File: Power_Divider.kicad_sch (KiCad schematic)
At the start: 31 parts, among them J86 Molex 73251-1153, J93 PIC-S-201F, P602 CONUFL001-SMD-T, P603 CONUFL001-SMD-T, P604 CONUFL001-SMD-T, P609 CONUFL001-SMD-T, U604 RBP-140+, U87 QPL9547

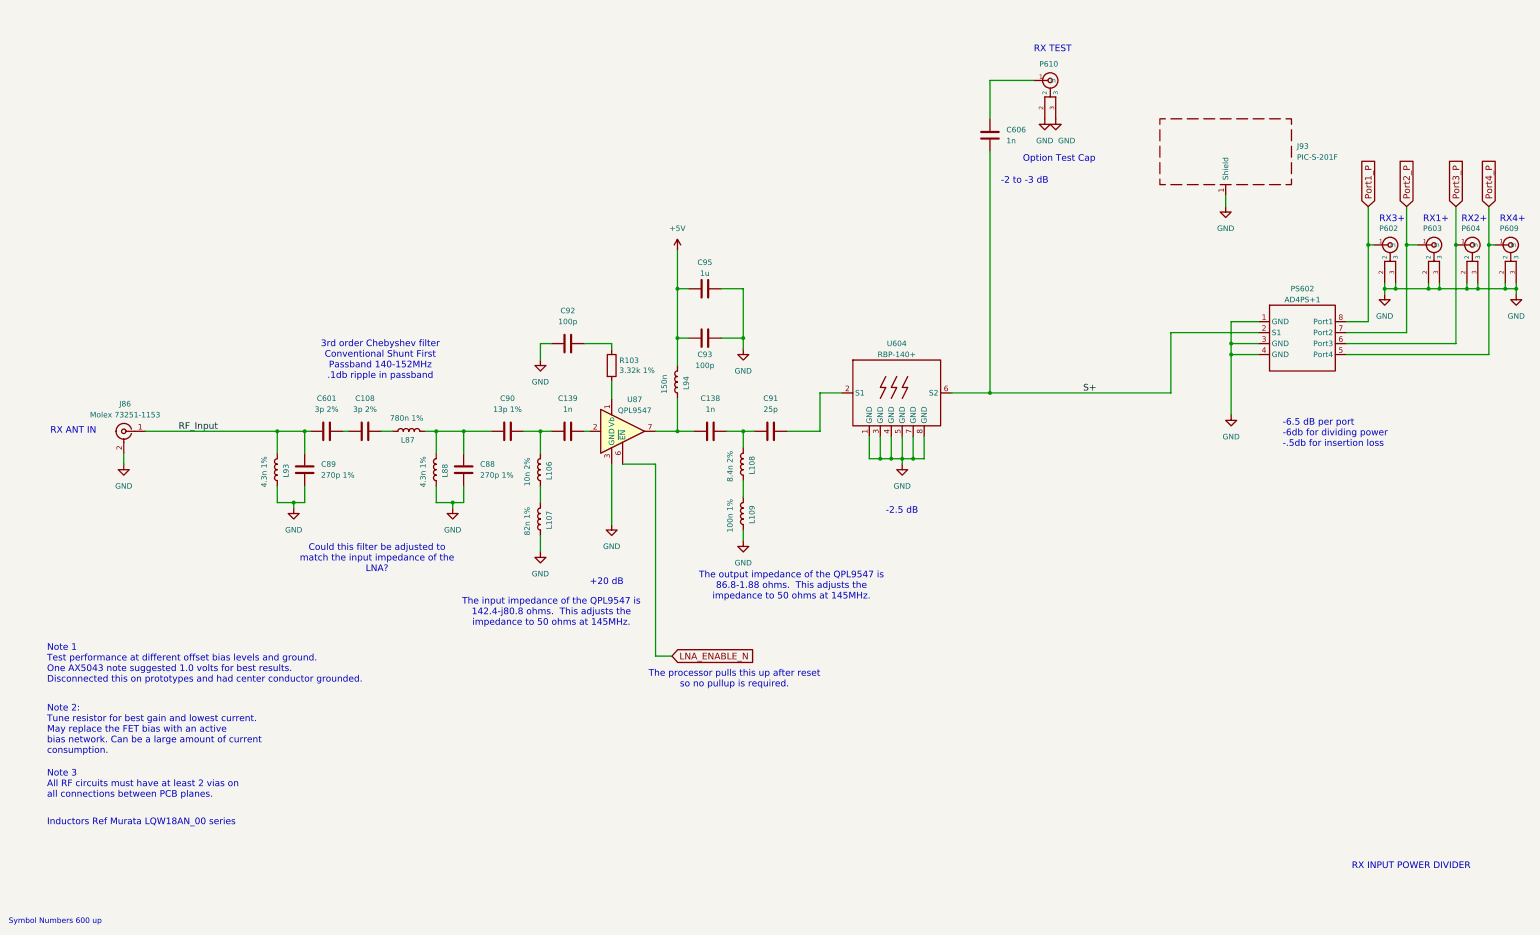
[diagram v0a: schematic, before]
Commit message: Re-annotate all parts
And get rid of the per-sheet annotation remarks.

Signed-off-by: Corey Minyard <corey@minyard.net>
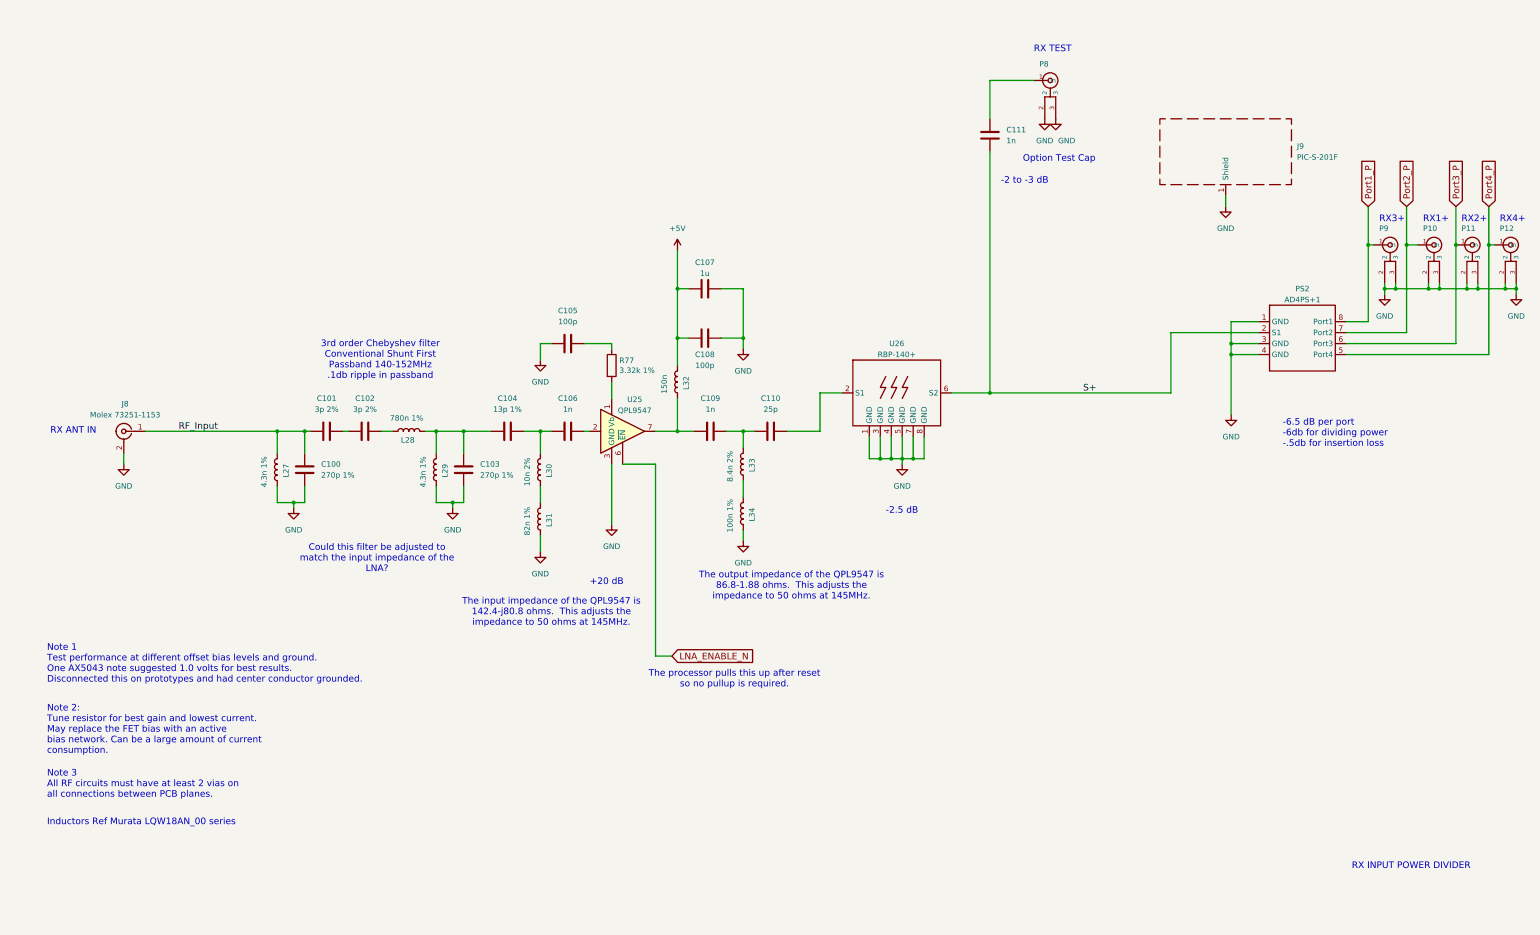
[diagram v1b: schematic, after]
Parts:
- renumbered C89 to C100, C601 to C101, C108 to C102, C88 to C103, C90 to C104, C92 to C105, C139 to C106, C95 to C107, C93 to C108, C138 to C109, C91 to C110, C606 to C111, J86 to J8, J93 to J9, L93 to L27, L87 to L28, L88 to L29, L106 to L30, L107 to L31, L94 to L32, L108 to L33, L109 to L34, P603 to P10, P604 to P11, P609 to P12, P610 to P8, P602 to P9, PS602 to PS2, R103 to R77, U87 to U25, U604 to U26
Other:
- note removed: "Symbol Numbers 600 up"

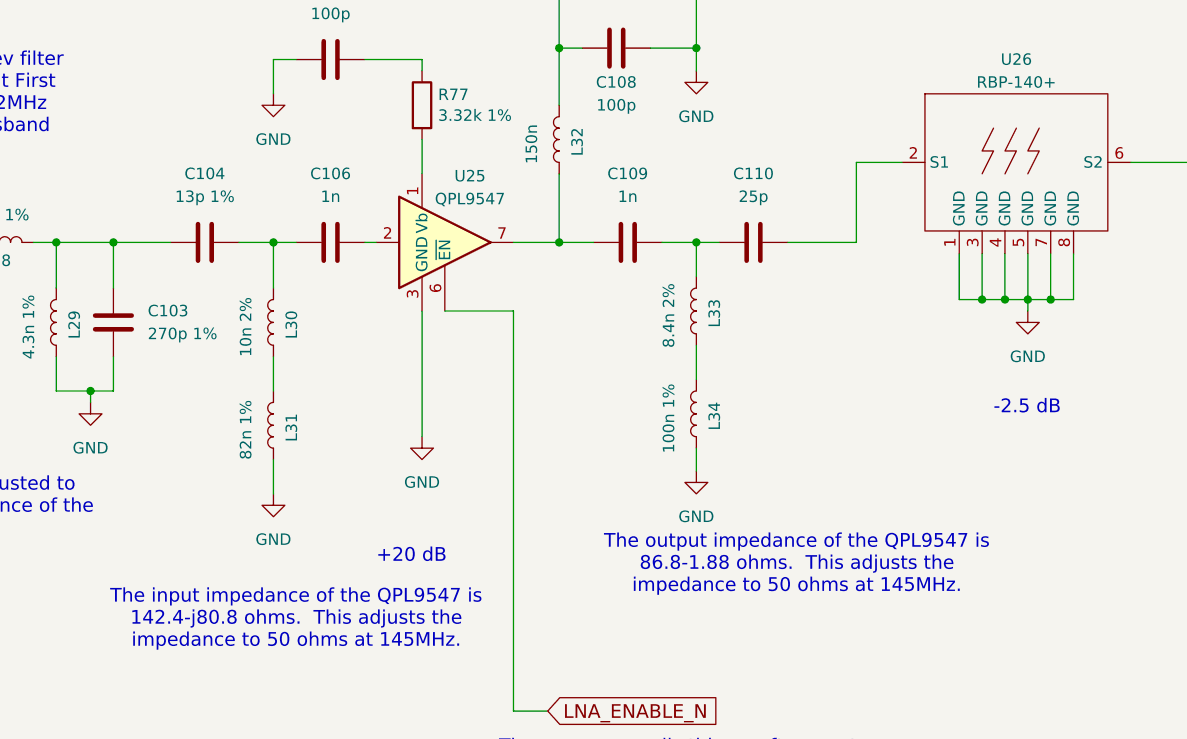
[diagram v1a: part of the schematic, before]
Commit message: Rework the LNA impedance matching
Signed-off-by: Corey Minyard <corey@minyard.net>
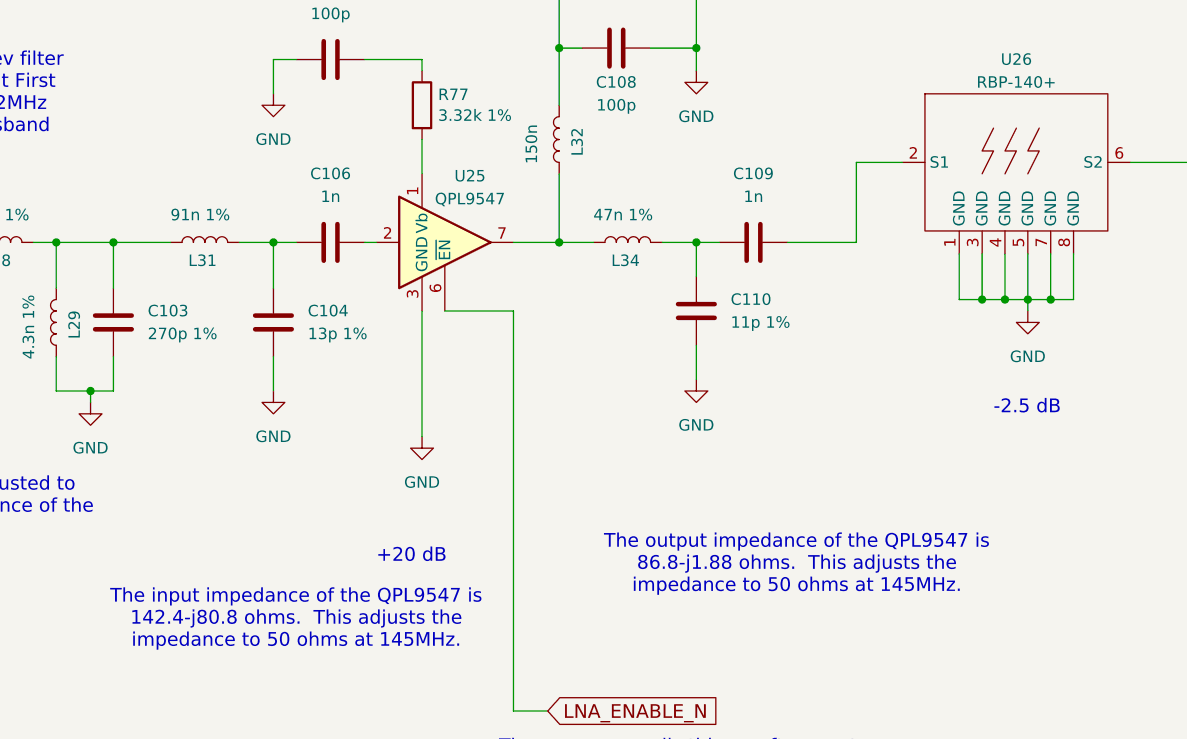
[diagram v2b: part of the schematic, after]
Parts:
- removed L30: 10n 2%, Inductor_SMD:L_0402_1005Metric_Pad0.77x0.64mm_HandSolder, symbol Device:L
- removed L33: 8.4n 2%, Inductor_SMD:L_0402_1005Metric_Pad0.77x0.64mm_HandSolder, symbol Device:L
- C110: value 25p -> 11p 1%
- L31: value 82n 1% -> 91n 1%
- L34: value 100n 1% -> 47n 1%
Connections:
- net GND: now also C104.2, C110.1; no longer L31.2, L34.2
- net at L31.1: now also C104.1, C106.2
- net at L32.2, U25.7: now also L34.2; no longer C109.2
- net at C109.1: now also U26.2 (S1); no longer C110.2
- net at C103.2, L28.1, L29.1: now also L31.2; no longer C104.2
- net at L34.1: now also C109.2, C110.2
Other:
- note added: "The output impedance of the QPL9547 is 86.8-j1.88 ohms. This adjusts the impedance to 50 ohms at 145MHz."
- note removed: "The output impedance of the QPL9547 is 86.8-1.88 ohms. This adjusts the impedance to 50 ohms at 145MHz."
- moved on the sheet: C104, C109, C110, L31, L34

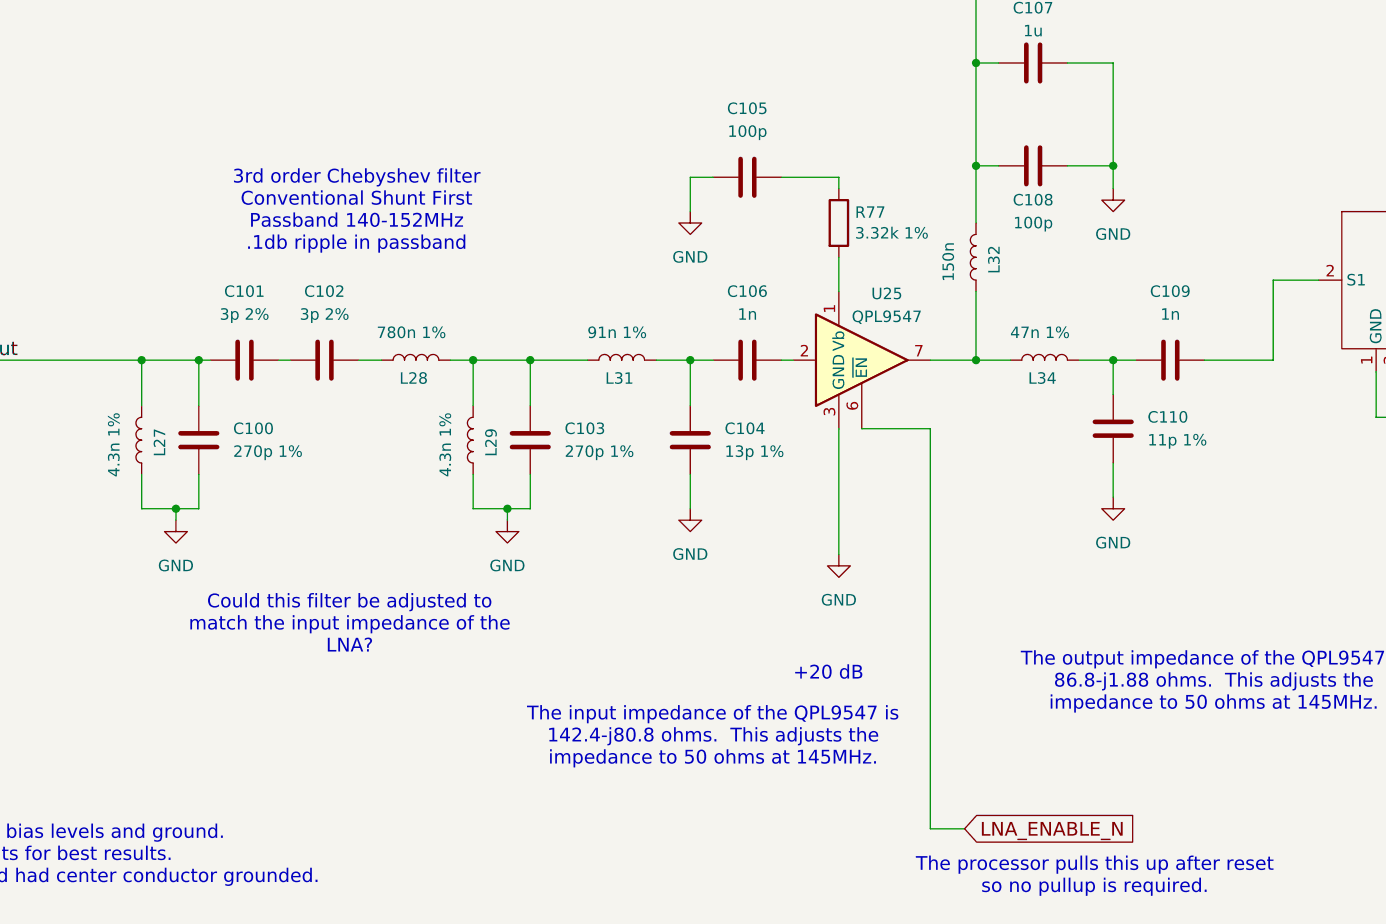
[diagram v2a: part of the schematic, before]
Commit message: More cleanup around the LNA
Had the C/L order on the output impedance match wrong.

Change the double 3pf caps to a 1.5pf, I think a suitable one can be
found.

Signed-off-by: Corey Minyard <corey@minyard.net>
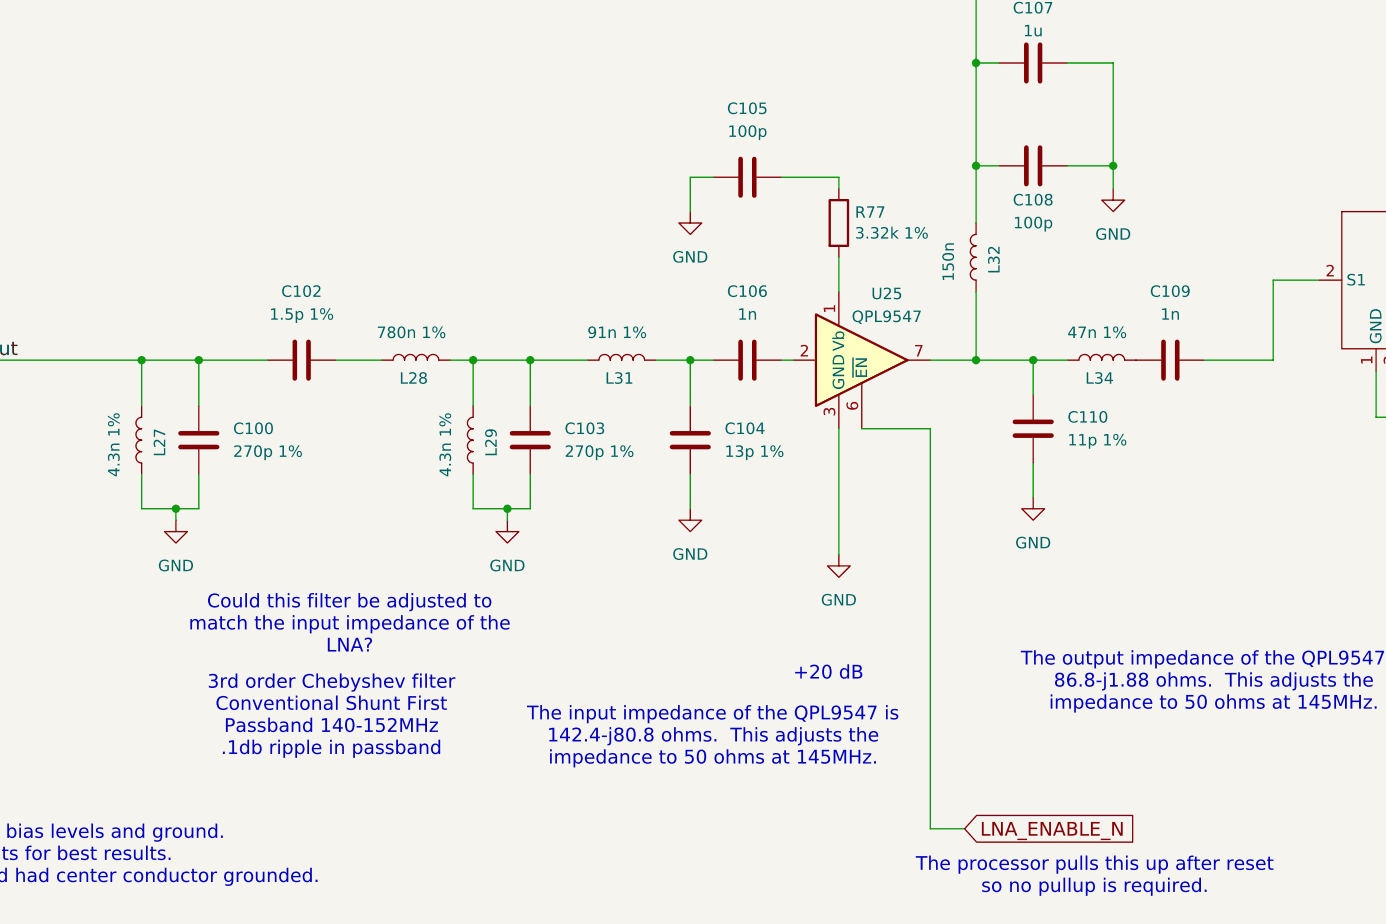
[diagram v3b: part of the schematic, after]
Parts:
- removed C101: 3p 2%, Capacitor_SMD:C_0402_1005Metric_Pad0.74x0.62mm_HandSolder, symbol Device:C
- C102: value 3p 2% -> 1.5p 1%
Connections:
- net RF_Input: now also C102.2
- net at L32.2, L34.2, U25.7: now also C110.2
- net at C109.2, L34.1: no longer C110.2
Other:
- moved on the sheet: C102, C110, L34
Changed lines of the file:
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@@
 	(text "3rd order Chebyshev filter\nConventional Shunt First\nPassband 140-152MHz\n.1db ripple in passband\n"
 		(exclude_from_sim no)
-		(at 105.156 127 0)
+		(at 102.362 183.134 0)
 		(effects
 			(font
@@
 	)
 	(junction
+		(at 87.63 143.51)
+		(diameter 0)
+		(color 0 0 0 0)
+	)
+	(junction
 		(at 302.26 125.73)
 		(diameter 0)
@@
 	)
 	(junction
-		(at 189.23 143.51)
+		(at 180.34 143.51)
 		(diameter 0)
 		(color 0 0 0 0)
@@
 	)
 	(junction
-		(at 87.63 143.51)
-		(diameter 0)
-		(color 0 0 0 0)
-	)
-	(junction
 		(at 246.38 134.62)
 		(diameter 0)
@@
 	(wire
 		(pts
-			(xy 189.23 143.51) (xy 191.77 143.51)
+			(xy 180.34 143.51) (xy 184.15 143.51)
 		)
 		(stroke
@@
 	(wire
 		(pts
-			(xy 189.23 143.51) (xy 189.23 147.32)
+			(xy 180.34 143.51) (xy 180.34 147.32)
 		)
 		(stroke
@@
 	(wire
 		(pts
+			(xy 87.63 143.51) (xy 95.25 143.51)
+		)
+		(stroke
+			(width 0)
+			(type default)
+		)
+	)
+	(wire
+		(pts
 			(xy 328.93 120.65) (xy 342.9 120.65)
 		)
@@
 	(wire
 		(pts
-			(xy 105.41 143.51) (xy 107.95 143.51)
+			(xy 102.87 143.51) (xy 107.95 143.51)
 		)
 		(stroke
@@
 	(wire
 		(pts
-			(xy 189.23 154.94) (xy 189.23 158.75)
+			(xy 180.34 154.94) (xy 180.34 158.75)
 		)
 		(stroke
@@
 	(wire
 		(pts
-			(xy 185.42 143.51) (xy 189.23 143.51)
-		)
-		(stroke
-			(width 0)
-			(type default)
-		)
-	)
-	(wire
-		(pts
 			(xy 142.24 156.21) (xy 142.24 160.02)
 		)
@@
 	(wire
 		(pts
-			(xy 173.99 143.51) (xy 177.8 143.51)
+			(xy 173.99 143.51) (xy 180.34 143.51)
 		)
 		(stroke
@@
 	(wire
 		(pts
-			(xy 87.63 143.51) (xy 88.9 143.51)
-		)
-		(stroke
-			(width 0)
-			(type default)
-		)
-	)
-	(wire
-		(pts
 			(xy 168.91 151.13) (xy 168.91 195.58)
 		)
@@
 	(wire
 		(pts
-			(xy 96.52 143.51) (xy 97.79 143.51)
-		)
-		(stroke
-			(width 0)
-			(type default)
-		)
-	)
-	(wire
-		(pts
 			(xy 223.52 144.78) (xy 223.52 149.86)
 		)
@@
 	(symbol
 		(lib_id "power:GND")
-		(at 189.23 158.75 0)
+		(at 180.34 158.75 0)
 		(unit 1)
 		(exclude_from_sim no)
@@
 		(fields_autoplaced yes)
 		(property "Reference" "#PWR0212"
-			(at 189.23 165.1 0)
+			(at 180.34 165.1 0)
 			(effects
 				(font
@@
 		)
 		(property "Value" "GND"
-			(at 189.23 163.83 0)
+			(at 180.34 163.83 0)
 			(effects
 				(font
@@
 		)
 		(property "Footprint" ""
-			(at 189.23 158.75 0)
+			(at 180.34 158.75 0)
 			(effects
 				(font
@@
 		)
 		(property "Datasheet" ""
-			(at 189.23 158.75 0)
+			(at 180.34 158.75 0)
 			(effects
 				(font
@@
 		)
 		(property "Description" ""
-			(at 189.23 158.75 0)
+			(at 180.34 158.75 0)
 			(effects
 				(font
@@
 	(symbol
 		(lib_id "Device:C")
-		(at 189.23 151.13 180)
+		(at 180.34 151.13 180)
 		(unit 1)
 		(exclude_from_sim no)
@@
 		(fields_autoplaced yes)
 		(property "Reference" "C110"
-			(at 193.04 149.8599 0)
+			(at 184.15 149.8599 0)
 			(effects
 				(font
@@
 		)
 		(property "Value" "11p 1%"
-			(at 193.04 152.3999 0)
+			(at 184.15 152.3999 0)
 			(effects
 				(font
@@
 		)
 		(property "Footprint" "Capacitor_SMD:C_0402_1005Metric_Pad0.74x0.62mm_HandSolder"
-			(at 188.2648 147.32 0)
+			(at 179.3748 147.32 0)
 			(effects
 				(font
@@
 		)
 		(property "Datasheet" "~"
-			(at 189.23 151.13 0)
+			(at 180.34 151.13 0)
 			(effects
 				(font
@@
 		)
 		(property "Description" ""
-			(at 189.23 151.13 0)
+			(at 180.34 151.13 0)
 			(effects
 				(font
@@
 	(symbol
 		(lib_id "Device:L")
-		(at 181.61 143.51 270)
+		(at 187.96 143.51 270)
 		(mirror x)
 		(unit 1)
@@
 		(dnp no)
 		(property "Reference" "L34"
-			(at 181.356 145.542 90)
+			(at 187.706 145.542 90)
 			(effects
 				(font
@@
 		)
 		(property "Value" "47n 1%"
-			(at 181.102 140.462 90)
+			(at 187.452 140.462 90)
 			(effects
 				(font
@@
 		)
 		(property "Footprint" "Inductor_SMD:L_0402_1005Metric_Pad0.77x0.64mm_HandSolder"
-			(at 181.61 143.51 0)
+			(at 187.96 143.51 0)
 			(effects
 				(font
@@
 		)
 		(property "Datasheet" "~"
-			(at 181.61 143.51 0)
+			(at 187.96 143.51 0)
 			(effects
 				(font
@@
 		)
 		(property "Description" ""
-			(at 181.61 143.51 0)
+			(at 187.96 143.51 0)
 			(effects
 				(font
@@
 	(symbol
 		(lib_id "Device:C")
-		(at 101.6 143.51 270)
+		(at 99.06 143.51 270)
 		(unit 1)
 		(exclude_from_sim no)
@@
 		(fields_autoplaced yes)
 		(property "Reference" "C102"
-			(at 101.6 135.89 90)
+			(at 99.06 135.89 90)
 			(effects
 				(font
@@
 			)
 		)
-		(property "Value" "3p 2%"
-			(at 101.6 138.43 90)
+		(property "Value" "1.5p 1%"
+			(at 99.06 138.43 90)
 			(effects
 				(font
@@
 		)
 		(property "Footprint" "Capacitor_SMD:C_0402_1005Metric_Pad0.74x0.62mm_HandSolder"
-			(at 97.79 144.4752 0)
+			(at 95.25 144.4752 0)
 			(effects
 				(font
@@
 		)
 		(property "Datasheet" "~"
-			(at 101.6 143.51 0)
+			(at 99.06 143.51 0)
 			(effects
 				(font
@@
 		)
 		(property "Description" ""
-			(at 101.6 143.51 0)
+			(at 99.06 143.51 0)
 			(effects
 				(font
@@
 					(unit 1)
 				)
-			)
-		)
-	)
-	(symbol
-		(lib_id "Device:C")
-		(at 92.71 143.51 270)
-		(unit 1)
-		(exclude_from_sim no)
-		(in_bom yes)
-		(on_board yes)
-		(dnp no)
-		(fields_autoplaced yes)
-		(property "Reference" "C101"
-			(at 92.71 135.89 90)
-			(effects
-				(font
-					(size 1.27 1.27)
-				)
-			)
-		)
-		(property "Value" "3p 2%"
-			(at 92.71 138.43 90)
-			(effects
-				(font
-					(size 1.27 1.27)
-				)
-			)
-		)
-		(property "Footprint" "Capacitor_SMD:C_0402_1005Metric_Pad0.74x0.62mm_HandSolder"
-			(at 88.9 144.4752 0)
-			(effects
-				(font
-					(size 1.27 1.27)
-				)
-				(hide yes)
-			)
-		)
-		(property "Datasheet" "~"
-			(at 92.71 143.51 0)
-			(effects
-				(font
-					(size 1.27 1.27)
-				)
-				(hide yes)
-			)
-		)
-		(property "Description" ""
-			(at 92.71 143.51 0)
-			(effects
-				(font
-					(size 1.27 1.27)
-				)
-			)
-		)
-		(pin "1"
-		)
-		(pin "2"
-		)
-		(instances
-			(project "PacSat_AFSK"
-				(path "/cc9f42d2-6985-41ac-acab-5ab7b01c5b38/9af0eacb-5211-4e23-85d7-9c1805bbe6a4"
-					(reference "C101")
-					(unit 1)
-				)
